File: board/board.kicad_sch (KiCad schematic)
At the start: 3 parts, among them J1 001_I2C, J2 011_GPIO

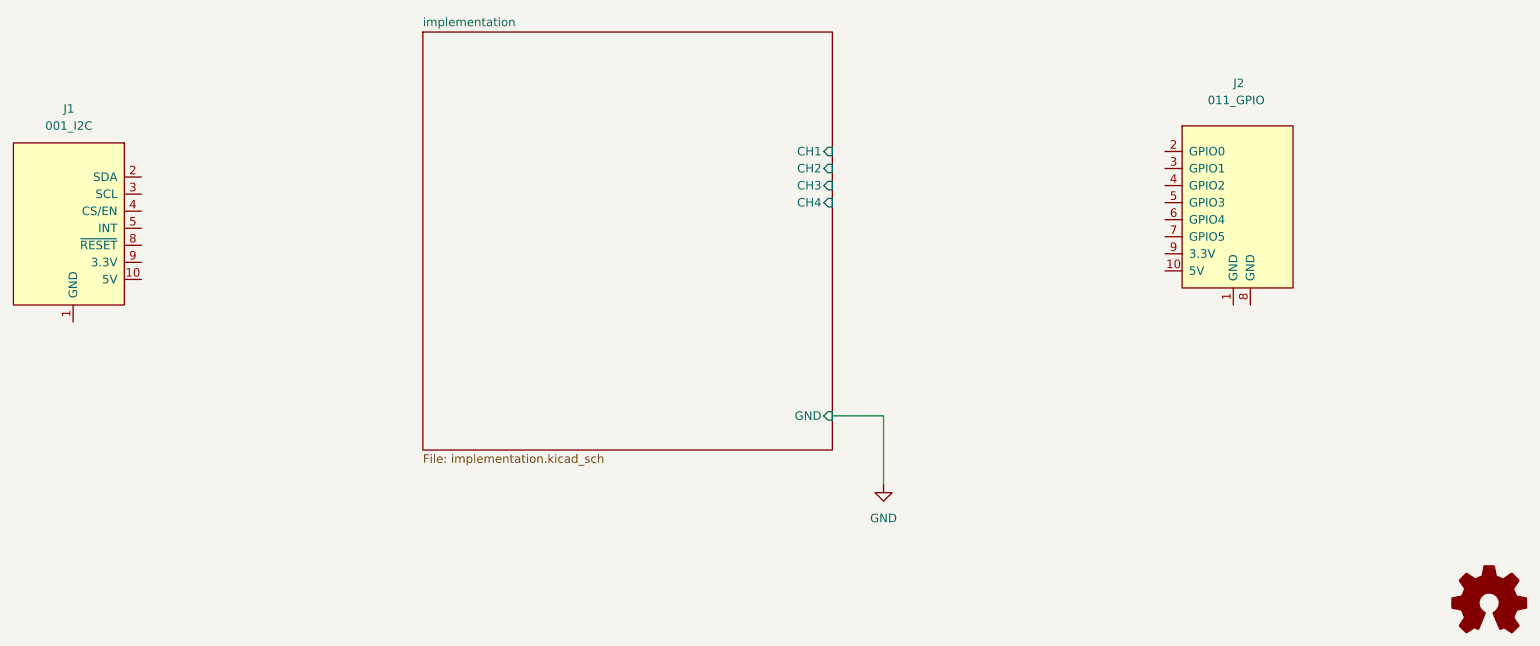
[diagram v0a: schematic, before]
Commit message: Add footprint, symbol and 3D modell | Add parts for reference cicuit
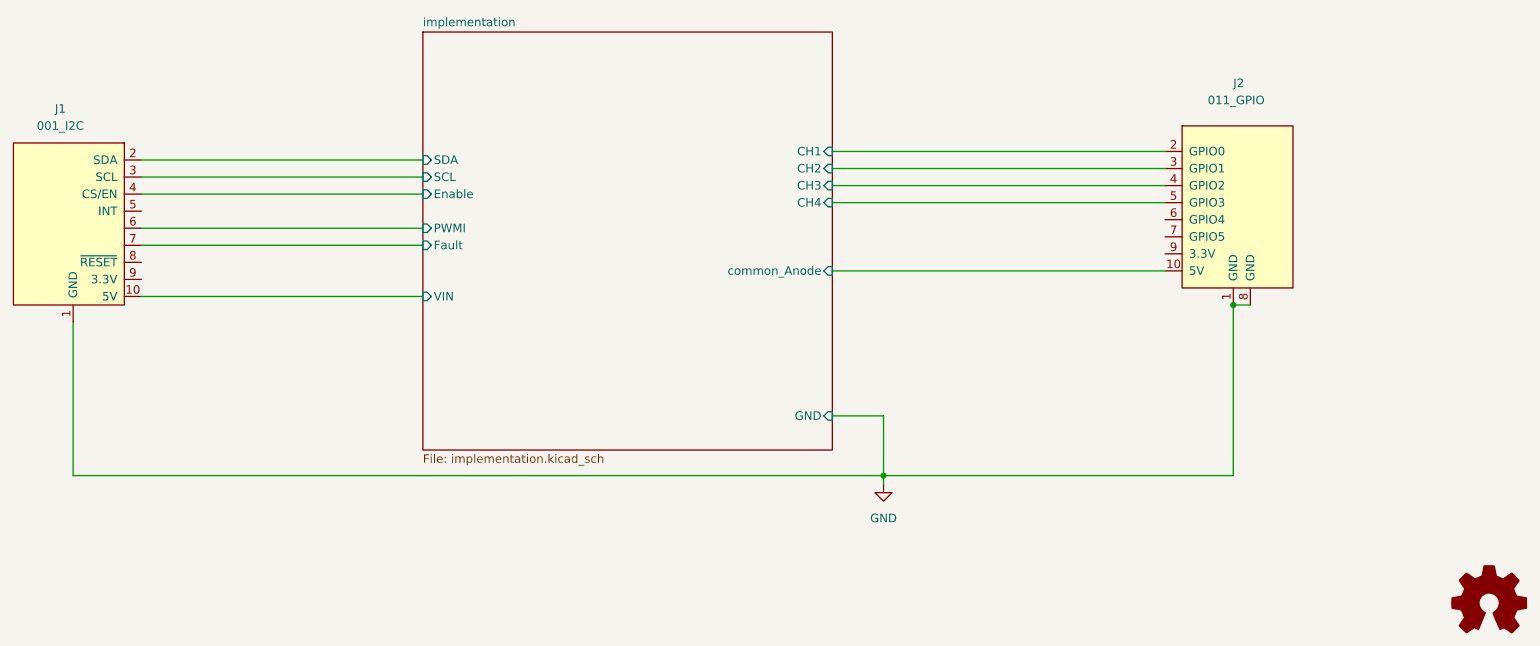
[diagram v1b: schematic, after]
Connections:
- net GND: now also J1.1 (GND), J2.1 (GND), J2.8 (GND)
- net implementation/CH1: now also J2.2 (GPIO0)
- net implementation/CH2: now also J2.3 (GPIO1)
- net implementation/CH3: now also J2.4 (GPIO2)
- net implementation/CH4: now also J2.5 (GPIO3)
- net implementation/VIN: now reaches J1.10 (5V)
- net implementation/SDA: now reaches J1.2 (SDA)
- net implementation/SCL: now reaches J1.3 (SCL)
- net implementation/Enable: now reaches J1.4 (CS/EN)
- net implementation/common_Anode: now reaches J2.10 (5V)
- new net implementation/Fault: J1.7
- new net implementation/PWMI: J1.6
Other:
- sheet implementation ports: added Enable, Fault, PWMI, SCL, SDA, VIN, common_Anode; removed none

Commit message: Add routing
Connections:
- net implementation/CH1: now also J2.5 (GPIO3); no longer J2.2 (GPIO0)
- net implementation/CH2: now also J2.4 (GPIO2); no longer J2.3 (GPIO1)
- net implementation/CH3: now also J2.3 (GPIO1); no longer J2.4 (GPIO2)
- net implementation/CH4: now also J2.2 (GPIO0); no longer J2.5 (GPIO3)

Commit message: Update PCB
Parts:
- added CS1, SCL1, SDA1, TP8: TestPoint, TestPoint:TestPoint_Pad_D1.0mm, symbol Connector:TestPoint
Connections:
- net implementation/Enable: now also CS1.1
- net implementation/PWMI: now also TP8.1
- net implementation/SCL: now also SCL1.1
- net implementation/SDA: now also SDA1.1
- net 3.3V: now reaches J1.9 (3.3V)
- net 3.3V: now also J2.9 (3.3V)
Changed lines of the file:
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@@
   (junction (at 182.88 138.43) (diameter 0) (color 0 0 0 0)
   )
+  (junction (at 82.55 91.44) (diameter 0) (color 0 0 0 0)
+  )
   (junction (at 234.95 113.03) (diameter 0) (color 0 0 0 0)
   )
+  (junction (at 92.71 101.6) (diameter 0) (color 0 0 0 0)
+  )
+  (junction (at 99.06 93.98) (diameter 0) (color 0 0 0 0)
+  )
+  (junction (at 78.74 96.52) (diameter 0) (color 0 0 0 0)
+  )
   (wire (pts (xy 218.44 95.25) (xy 218.44 92.71))
     (stroke (width 0) (type default))
@@
     (stroke (width 0) (type default))
   )
+  (wire (pts (xy 82.55 91.44) (xy 114.3 91.44))
+    (stroke (width 0) (type default))
+  )
   (wire (pts (xy 193.04 91.44) (xy 177.8 91.44))
     (stroke (width 0) (type default))
   )
-  (wire (pts (xy 72.39 91.44) (xy 114.3 91.44))
+  (wire (pts (xy 99.06 93.98) (xy 114.3 93.98))
+    (stroke (width 0) (type default))
+  )
+  (wire (pts (xy 72.39 91.44) (xy 82.55 91.44))
     (stroke (width 0) (type default))
   )
@@
     (stroke (width 0) (type default))
   )
-  (wire (pts (xy 72.39 101.6) (xy 114.3 101.6))
+  (wire (pts (xy 72.39 101.6) (xy 92.71 101.6))
+    (stroke (width 0) (type default))
+  )
+  (wire (pts (xy 92.71 101.6) (xy 114.3 101.6))
     (stroke (width 0) (type default))
   )
@@
     (stroke (width 0) (type default))
   )
+  (wire (pts (xy 78.74 96.52) (xy 114.3 96.52))
+    (stroke (width 0) (type default))
+  )
   (wire (pts (xy 189.23 90.17) (xy 189.23 97.79))
     (stroke (width 0) (type default))
@@
     (stroke (width 0) (type default))
   )
-  (wire (pts (xy 72.39 93.98) (xy 114.3 93.98))
+  (wire (pts (xy 72.39 93.98) (xy 99.06 93.98))
     (stroke (width 0) (type default))
   )
@@
     (stroke (width 0) (type default))
   )
-  (wire (pts (xy 72.39 96.52) (xy 114.3 96.52))
+  (wire (pts (xy 72.39 96.52) (xy 78.74 96.52))
     (stroke (width 0) (type default))
   )
@@
   (wire (pts (xy 220.98 93.98) (xy 220.98 95.25))
     (stroke (width 0) (type default))
+  )
+  (global_label "3.3V" (shape input) (at 72.39 109.22 0) (fields_autoplaced)
+    (effects (font (size 1.27 1.27)) (justify left))
+    (property "Intersheetrefs" "${INTERSHEET_REFS}" (at 79.4082 109.22 0)
+      (effects (font (size 1.27 1.27)) (justify left) hide)
+    )
+  )
+  (global_label "3.3V" (shape output) (at 224.79 105.41 180) (fields_autoplaced)
+    (effects (font (size 1.27 1.27)) (justify right))
+    (property "Intersheetrefs" "${INTERSHEET_REFS}" (at 217.7718 105.41 0)
+      (effects (font (size 1.27 1.27)) (justify right) hide)
+    )
   )
   (symbol (lib_id "put_on_edge:001_I2C") (at 60.96 101.6 0) (mirror y) (unit 1)
@@
     )
   )
+  (symbol (lib_id "Connector:TestPoint") (at 92.71 101.6 0) (unit 1)
+    (in_bom yes) (on_board yes) (dnp no) (fields_autoplaced)
+    (property "Reference" "TP8" (at 95.25 97.028 0)
+      (effects (font (size 1.27 1.27)) (justify left))
+    )
+    (property "Value" "TestPoint" (at 95.25 99.568 0)
+      (effects (font (size 1.27 1.27)) (justify left))
+    )
+    (property "Footprint" "TestPoint:TestPoint_Pad_D1.0mm" (at 97.79 101.6 0)
+      (effects (font (size 1.27 1.27)) hide)
+    )
+    (property "Datasheet" "~" (at 97.79 101.6 0)
+      (effects (font (size 1.27 1.27)) hide)
+    )
+    (pin "1")
+    (instances
+      (project "board"
+        (path "/57732dd3-1162-4c3f-88bd-31bf473d124d/767ce4c6-0e55-4543-92f0-34cb8237a544"
+          (reference "TP8") (unit 1)
+        )
+        (path "/57732dd3-1162-4c3f-88bd-31bf473d124d"
+          (reference "PWMI1") (unit 1)
+        )
+      )
+    )
+  )
+  (symbol (lib_id "Connector:TestPoint") (at 78.74 96.52 0) (unit 1)
+    (in_bom yes) (on_board yes) (dnp no) (fields_autoplaced)
+    (property "Reference" "CS1" (at 81.28 91.948 0)
+      (effects (font (size 1.27 1.27)) (justify left))
+    )
+    (property "Value" "TestPoint" (at 81.28 94.488 0)
+      (effects (font (size 1.27 1.27)) (justify left))
+    )
+    (property "Footprint" "TestPoint:TestPoint_Pad_D1.0mm" (at 83.82 96.52 0)
+      (effects (font (size 1.27 1.27)) hide)
+    )
+    (property "Datasheet" "~" (at 83.82 96.52 0)
+      (effects (font (size 1.27 1.27)) hide)
+    )
+    (pin "1")
+    (instances
+      (project "board"
+        (path "/57732dd3-1162-4c3f-88bd-31bf473d124d"
+          (reference "CS1") (unit 1)
+        )
+      )
+    )
+  )
   (symbol (lib_id "put_on_edge:011_GPIO") (at 236.22 99.06 0) (unit 1)
     (in_bom yes) (on_board yes) (dnp no)
@@
         )
       )
+    )
+  )
+  (symbol (lib_id "Connector:TestPoint") (at 82.55 91.44 0) (unit 1)
+    (in_bom yes) (on_board yes) (dnp no) (fields_autoplaced)
+    (property "Reference" "SDA1" (at 85.09 86.868 0)
+      (effects (font (size 1.27 1.27)) (justify left))
+    )
+    (property "Value" "TestPoint" (at 85.09 89.408 0)
+      (effects (font (size 1.27 1.27)) (justify left))
+    )
+    (property "Footprint" "TestPoint:TestPoint_Pad_D1.0mm" (at 87.63 91.44 0)
+      (effects (font (size 1.27 1.27)) hide)
+    )
+    (property "Datasheet" "~" (at 87.63 91.44 0)
+      (effects (font (size 1.27 1.27)) hide)
+    )
+    (pin "1")
+    (instances
+      (project "board"
+        (path "/57732dd3-1162-4c3f-88bd-31bf473d124d"
+          (reference "SDA1") (unit 1)
+        )
+      )
+    )
+  )
+  (symbol (lib_id "Connector:TestPoint") (at 99.06 93.98 0) (unit 1)
+    (in_bom yes) (on_board yes) (dnp no) (fields_autoplaced)
+    (property "Reference" "SCL1" (at 101.6 89.408 0)
+      (effects (font (size 1.27 1.27)) (justify left))
+    )
+    (property "Value" "TestPoint" (at 101.6 91.948 0)
+      (effects (font (size 1.27 1.27)) (justify left))
+    )
+    (property "Footprint" "TestPoint:TestPoint_Pad_D1.0mm" (at 104.14 93.98 0)
+      (effects (font (size 1.27 1.27)) hide)
+    )
+    (property "Datasheet" "~" (at 104.14 93.98 0)
+      (effects (font (size 1.27 1.27)) hide)
+    )
+    (pin "1")
+    (instances
+      (project "board"
+        (path "/57732dd3-1162-4c3f-88bd-31bf473d124d"
+          (reference "SCL1") (unit 1)
+        )
+      )
